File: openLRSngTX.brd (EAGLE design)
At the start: 50 x 40 mm, 29 parts, among them IC1 RFM23BPSMD, J1 AVR_SPI_PRG_6PTH, Q1 MMBT2222, U1 ATMEGA328P, X1 BU-SMA-V, Y1 16MHz

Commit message: Add Open Hardware logo
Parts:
- added U$1: (no value), SparkFun-Aesthetics:OSHW-LOGO-L
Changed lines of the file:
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@@
 </element>
 <element name="R7" library="SparkFun-Resistors" package="0402-RES" value="1k" x="2.794" y="30.48" rot="R270"/>
+<element name="U$1" library="SparkFun-Aesthetics" package="OSHW-LOGO-L" value="" x="43.942" y="18.288" rot="MR0"/>
 </elements>
 <signals>

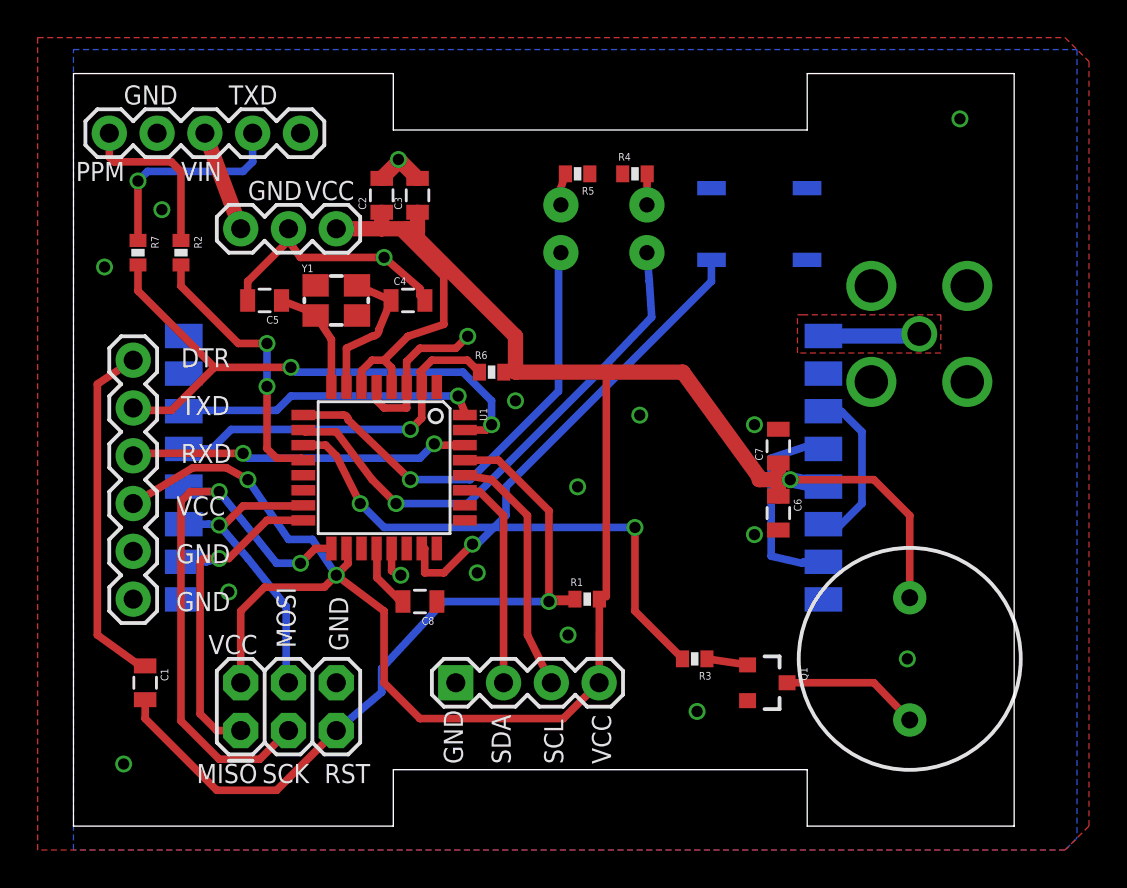
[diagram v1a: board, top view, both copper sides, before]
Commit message: Add mode switch header and room for the actual switch.
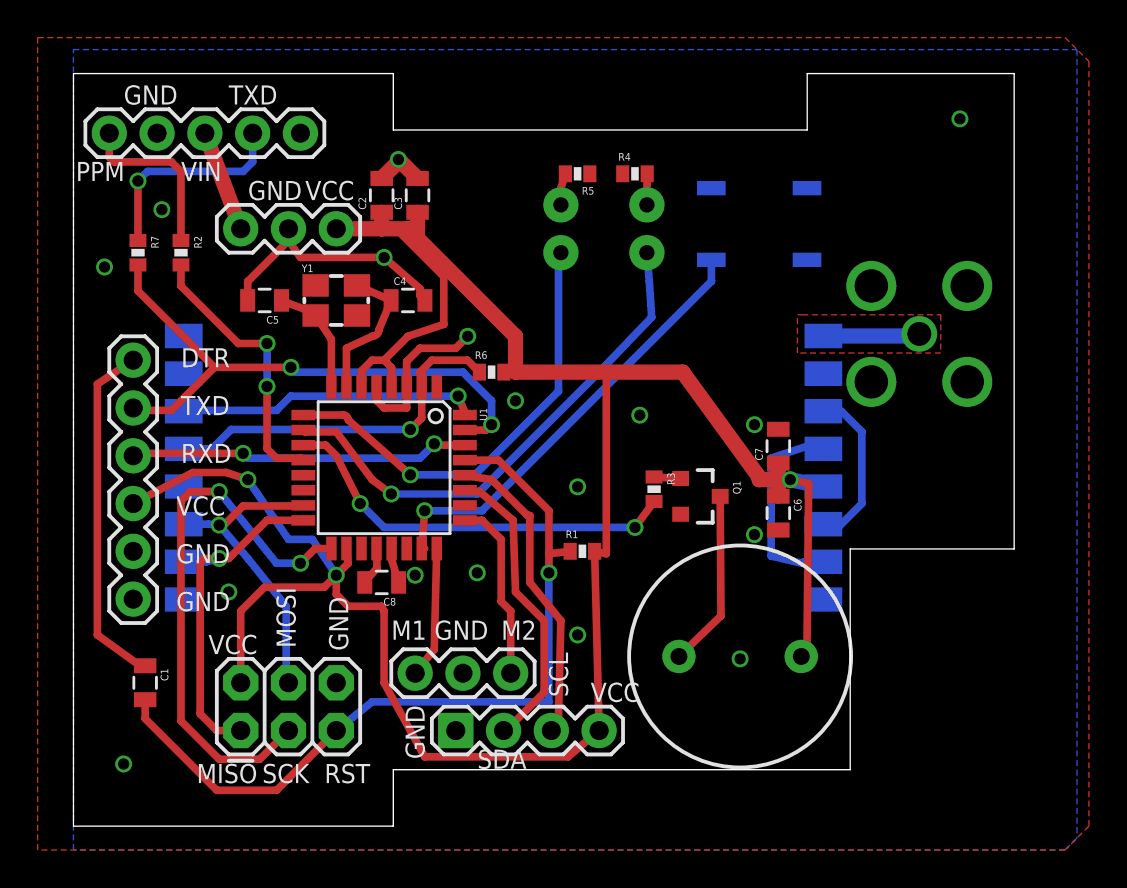
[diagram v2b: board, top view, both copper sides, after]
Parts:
- added JP5: mode, SparkFun-Connectors:1X03
- moved Q1 10.5 mm to (32.6, 17.5)
- moved R3 9.27 mm to (30.2, 17.9), turned to 270 degrees
- moved SG1 9.02 mm to (34.8, 9.02), turned to 0 degrees
- moved R1 2.55 mm to (26.4, 14.6)
- moved JP3 2.54 mm to (19.7, 5.08)
- moved C8 2.27 mm to (15.7, 13.0)
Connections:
- new net N$18: JP5.1, U1.24
- new net N$19: JP5.3, U1.25
- net GND: now also JP5.2
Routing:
- net N$19: track 0.00 -> 9.67 mm
- net N$18: track 0.00 -> 6.99 mm
- net N$4: track 28.0 -> 21.7 mm
- net SDA: track 11.5 -> 15.9 mm
- net VCC: track 126.0 -> 129.7 mm
- net SCL: track 13.3 -> 16.4 mm
- net N$6: track 7.36 -> 9.46 mm
- net N$15: track 25.1 -> 23.6 mm
- net N$14: track 3.45 -> 2.05 mm
- net N$5: track 2.18 -> 1.42 mm
- net /RESET: track 42.2 -> 42.8 mm
- net GND: track 26.8 -> 26.9 mm, vias 18 -> 17
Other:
- outline, holes or cut-outs redrawn
- board text added: "M1"
- board text added: "M2"

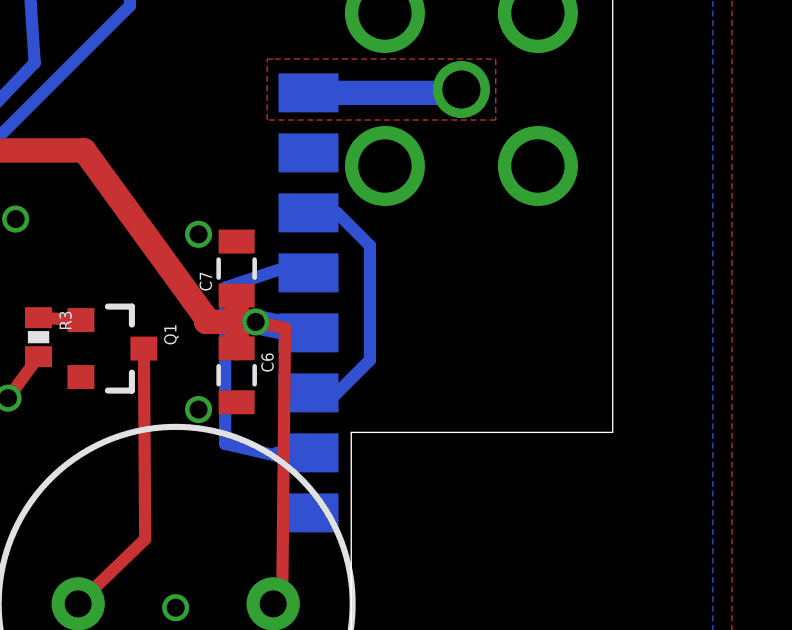
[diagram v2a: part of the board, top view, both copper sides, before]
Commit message: Add logo on other side too.
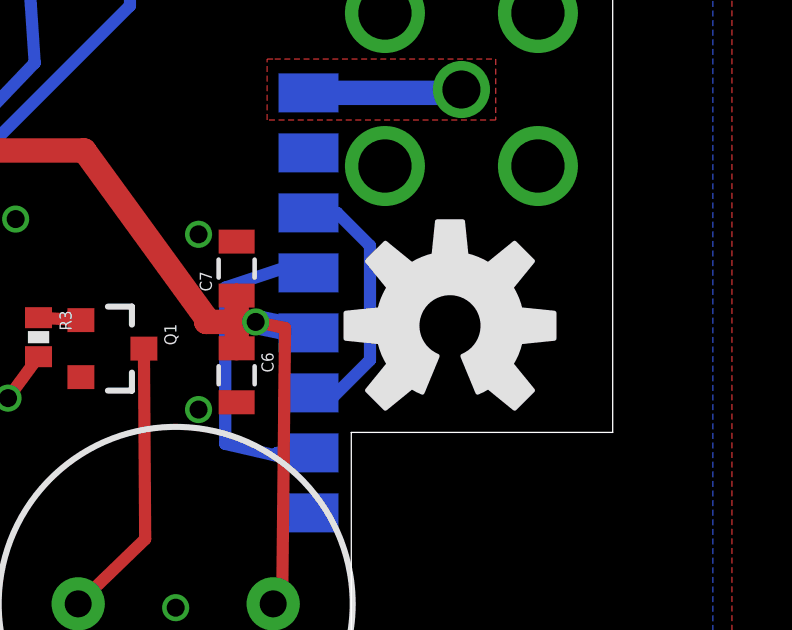
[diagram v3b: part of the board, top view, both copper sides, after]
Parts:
- added U$2: (no value), SparkFun-Aesthetics:OSHW-LOGO-L
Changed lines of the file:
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@@
 <element name="U$1" library="SparkFun-Aesthetics" package="OSHW-LOGO-L" value="" x="43.942" y="18.288" rot="MR0"/>
 <element name="JP5" library="SparkFun-Connectors" package="1X03" value="mode" x="17.526" y="8.128" smashed="yes"/>
+<element name="U$2" library="SparkFun-Aesthetics" package="OSHW-LOGO-L" value="" x="43.942" y="18.288"/>
 </elements>
 <signals>

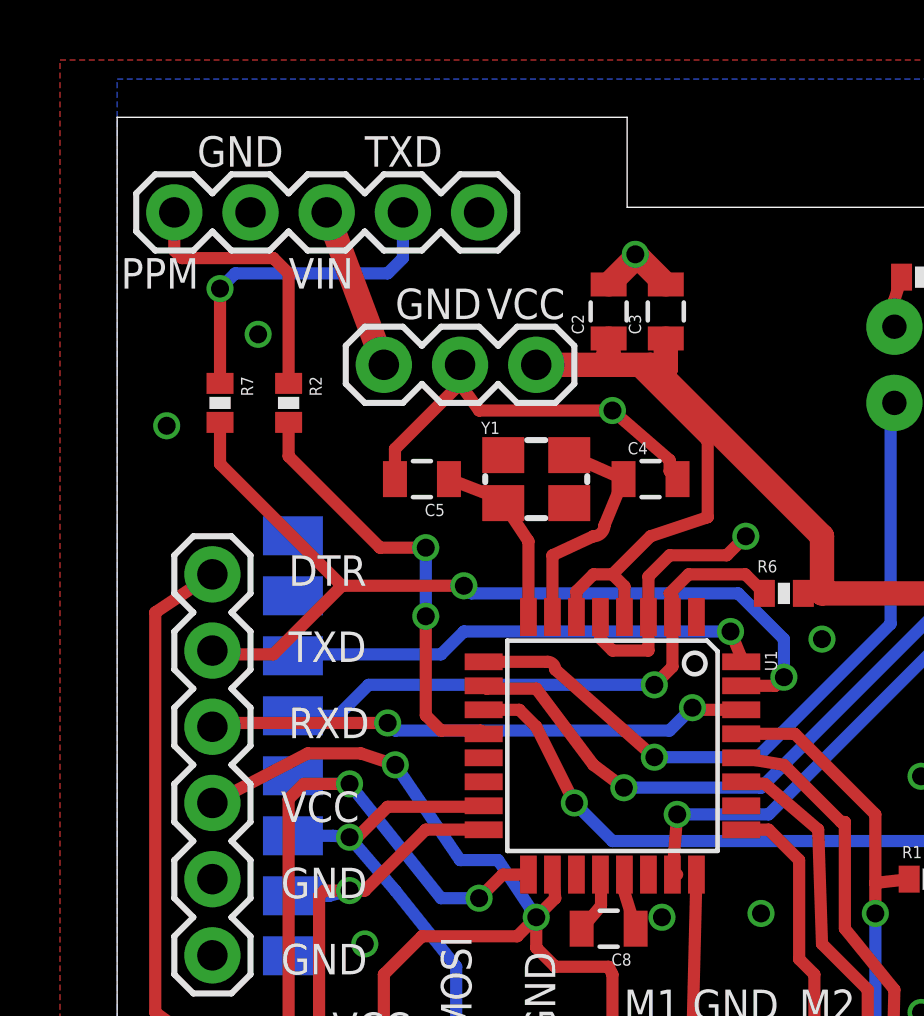
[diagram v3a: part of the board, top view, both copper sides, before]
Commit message: Added connection for RXD towards the radio. Connected xtal case to GND. Performed some routing cleanup.
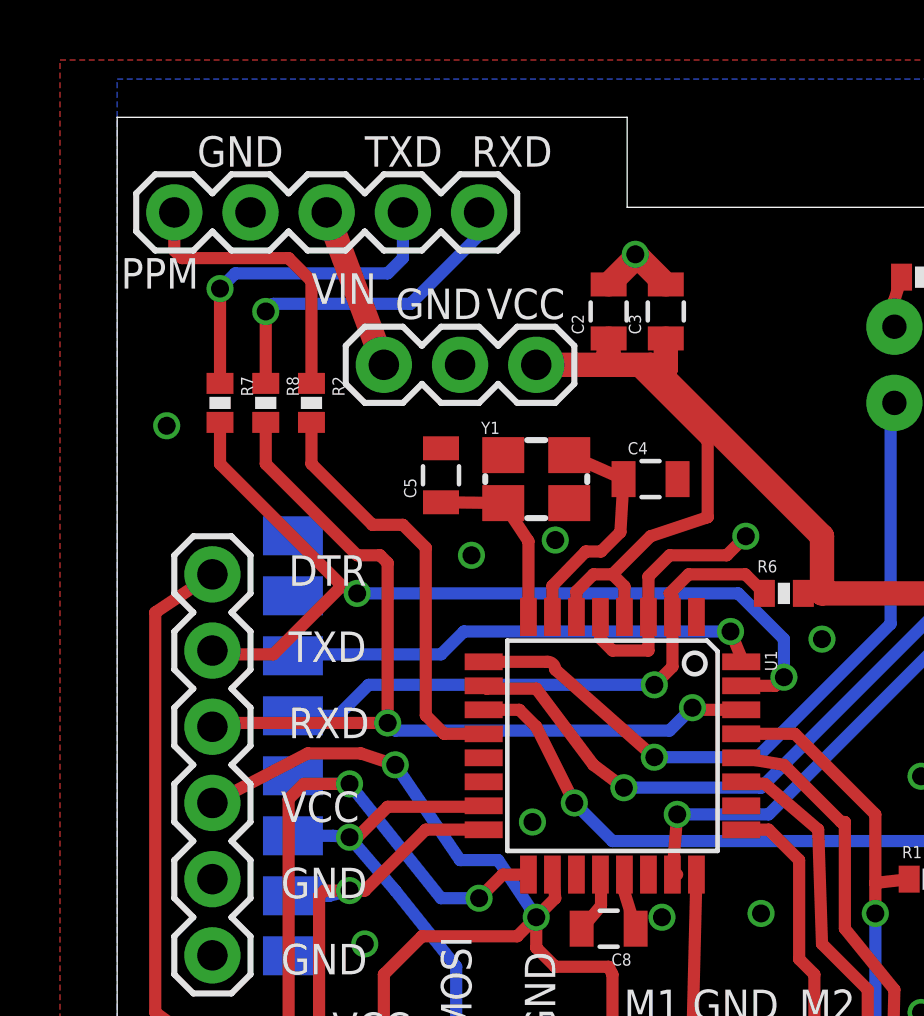
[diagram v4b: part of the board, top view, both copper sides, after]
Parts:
- added R8: 1k, SparkFun-Resistors:0402-RES
- moved R2 0.76 mm to (5.84, 30.5)
- moved C5 0.65 mm to (10.2, 28.1), turned to 90 degrees
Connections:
- new net N$20: JP1.5, R8.1
- net GND: now also Y1.2, Y1.4
- net RXD: now also R8.2
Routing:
- net GND: track 26.9 -> 13.4 mm, vias 17 -> 18
- net RXD: track 18.1 -> 30.3 mm
- net N$20: track 0.00 -> 11.3 mm, vias 0 -> 1
- net N$3: track 9.06 -> 9.68 mm
- net ICP: track 14.7 -> 14.1 mm, vias 2 -> 0
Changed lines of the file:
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@@
 <text x="-0.508" y="34.29" size="1.016" layer="25">PPM</text>
 <text x="2.032" y="38.354" size="1.016" layer="25">GND</text>
-<text x="5.08" y="34.29" size="1.016" layer="25">VIN</text>
+<text x="5.842" y="33.782" size="1.016" layer="25">VIN</text>
 <text x="7.62" y="38.354" size="1.016" layer="25">TXD</text>
 <text x="11.684" y="33.274" size="1.016" layer="25">VCC</text>
@@
 <text x="22.098" y="9.906" size="1.016" layer="25">M2</text>
 <text x="18.542" y="9.906" size="1.016" layer="25">GND</text>
+<text x="11.176" y="38.354" size="1.016" layer="25">RXD</text>
 </plain>
 <attributes>
@@
 <element name="Q1" library="SparkFun-DiscreteSemi" package="SOT23-3" value="MMBT2222" x="32.639" y="17.526" rot="R270"/>
 <element name="R1" library="SparkFun-Resistors" package="0402-RES" value="10k" x="26.416" y="14.605"/>
-<element name="R2" library="SparkFun-Resistors" package="0402-RES" value="1k" x="5.08" y="30.48" rot="R270"/>
+<element name="R2" library="SparkFun-Resistors" package="0402-RES" value="1k" x="5.842" y="30.48" rot="R270"/>
 <element name="R3" library="SparkFun-Resistors" package="0402-RES" value="1k" x="30.226" y="17.907" rot="R270"/>
 <element name="R4" library="SparkFun-Resistors" package="0402-RES" value="220R" x="29.21" y="34.671"/>
@@
 <element name="C3" library="SparkFun-Capacitors" package="0805" value="1uF" x="17.653" y="33.528" rot="R90"/>
 <element name="C4" library="SparkFun-Capacitors" package="0805" value="12pF" x="17.145" y="27.94"/>
-<element name="C5" library="SparkFun-Capacitors" package="0805" value="12pF" x="9.525" y="27.94" rot="R180"/>
+<element name="C5" library="SparkFun-Capacitors" package="0805" value="12pF" x="10.16" y="28.067" rot="R90"/>
 <element name="X1" library="con-coax" package="BU-SMA-V" value="BU-SMA-V" x="44.323" y="26.162" smashed="yes" rot="MR0">
 <attribute name="OC_NEWARK" value="unknown" x="44.323" y="26.162" size="1.778" layer="28" rot="MR0" display="off"/>
@@
 <element name="JP5" library="SparkFun-Connectors" package="1X03" value="mode" x="17.526" y="8.128" smashed="yes"/>
 <element name="U$2" library="SparkFun-Aesthetics" package="OSHW-LOGO-L" value="" x="43.942" y="18.288"/>
+<element name="R8" library="SparkFun-Resistors" package="0402-RES" value="1k" x="4.318" y="30.48" rot="R270"/>
 </elements>
 <signals>
@@
 <vertex x="-0.635" y="-1.27"/>
 </polygon>
-<wire x1="8.625" y1="27.94" x2="8.625" y2="28.945" width="0.4064" layer="1"/>
-<wire x1="8.625" y1="28.945" x2="10.795" y2="31.115" width="0.4064" layer="1"/>
-<wire x1="10.795" y1="31.75" x2="10.795" y2="31.115" width="0.4064" layer="1"/>
-<wire x1="10.795" y1="31.115" x2="11.43" y2="30.226" width="0.4064" layer="1"/>
-<wire x1="11.43" y1="30.226" x2="15.875" y2="30.226" width="0.4064" layer="1"/>
-<wire x1="15.875" y1="30.226" x2="17.78" y2="28.575" width="0.4064" layer="1"/>
-<wire x1="17.78" y1="28.575" x2="17.78" y2="28.205" width="0.4064" layer="1"/>
-<wire x1="17.78" y1="28.205" x2="18.045" y2="27.94" width="0.4064" layer="1"/>
-<via x="15.875" y="30.226" extent="1-16" drill="0.6"/>
 <wire x1="17.075" y1="23.3426" x2="17.075" y2="24.695" width="0.4064" layer="1"/>
 <wire x1="17.075" y1="24.695" x2="17.78" y2="25.4" width="0.4064" layer="1"/>
@@
 <via x="35.56" y="15.494" extent="1-16" drill="0.6"/>
 <via x="7.62" y="12.446" extent="1-16" drill="0.6"/>
-<via x="4.064" y="32.766" extent="1-16" drill="0.6"/>
 <via x="26.162" y="10.16" extent="1-16" drill="0.6"/>
 <via x="26.162" y="18.034" extent="1-16" drill="0.6"/>
@@
 <wire x1="16.275" y1="14.7574" x2="16.256" y2="14.224" width="0.4064" layer="1"/>
 <wire x1="16.256" y1="14.224" x2="16.648" y2="12.954" width="0.4064" layer="1"/>
+<contactref element="Y1" pad="4"/>
+<contactref element="Y1" pad="2"/>
+<contactref element="Y1" pad="4"/>
+<contactref element="Y1" pad="2"/>
+<via x="13.97" y="25.908" extent="1-16" drill="0.6"/>
+<via x="11.176" y="25.4" extent="1-16" drill="0.6"/>
+<via x="13.208" y="16.51" extent="1-16" drill="0.6"/>
 </signal>
 <signal name="VCC">
@@
 <wire x1="18.542" y1="20.32" x2="18.612" y2="20.25" width="0.4064" layer="1"/>
 <wire x1="18.612" y1="20.25" x2="20.1676" y2="20.25" width="0.4064" layer="1"/>
+<contactref element="R8" pad="2"/>
+<wire x1="4.318" y1="29.83" x2="4.318" y2="28.448" width="0.4064" layer="1"/>
+<wire x1="4.318" y1="28.448" x2="7.366" y2="25.4" width="0.4064" layer="1"/>
+<wire x1="7.366" y1="25.4" x2="8.128" y2="25.4" width="0.4064" layer="1"/>
+<wire x1="8.128" y1="25.4" x2="8.382" y2="25.146" width="0.4064" layer="1"/>
+<wire x1="8.382" y1="25.146" x2="8.382" y2="19.812" width="0.4064" layer="1"/>
 </signal>
 <signal name="TXD">
@@
 <wire x1="21.59" y1="21.336" x2="21.59" y2="22.606" width="0.4064" layer="16"/>
 <wire x1="21.59" y1="22.606" x2="20.066" y2="24.13" width="0.4064" layer="16"/>
-<wire x1="20.066" y1="24.13" x2="11.176" y2="24.13" width="0.4064" layer="16"/>
-<wire x1="11.176" y1="24.13" x2="10.922" y2="24.384" width="0.4064" layer="16"/>
-<via x="10.922" y="24.384" extent="1-16" drill="0.6"/>
-<wire x1="10.922" y1="24.384" x2="6.858" y2="24.384" width="0.4064" layer="1"/>
+<wire x1="20.066" y1="24.13" x2="7.366" y2="24.13" width="0.4064" layer="16"/>
+<via x="7.366" y="24.13" extent="1-16" drill="0.6"/>
+<wire x1="7.366" y1="24.13" x2="6.858" y2="24.384" width="0.4064" layer="1"/>
 <wire x1="6.858" y1="24.384" x2="4.572" y2="22.098" width="0.4064" layer="1"/>
 <wire x1="4.572" y1="22.098" x2="2.667" y2="22.098" width="0.4064" layer="1"/>
@@
 <contactref element="U1" pad="12"/>
 <contactref element="R2" pad="2"/>
-<wire x1="11.5824" y1="19.45" x2="11.4744" y2="19.558" width="0.4064" layer="1"/>
-<wire x1="11.4744" y1="19.558" x2="10.16" y2="19.558" width="0.4064" layer="1"/>
-<wire x1="10.16" y1="19.558" x2="9.652" y2="20.066" width="0.4064" layer="1"/>
-<wire x1="9.652" y1="20.066" x2="9.652" y2="23.368" width="0.4064" layer="1"/>
-<via x="9.652" y="23.368" extent="1-16" drill="0.6"/>
-<wire x1="9.652" y1="23.368" x2="9.652" y2="25.654" width="0.4064" layer="16"/>
-<via x="9.652" y="25.654" extent="1-16" drill="0.6"/>
-<wire x1="9.652" y1="25.654" x2="8.128" y2="25.654" width="0.4064" layer="1"/>
-<wire x1="8.128" y1="25.654" x2="5.08" y2="28.702" width="0.4064" layer="1"/>
-<wire x1="5.08" y1="28.702" x2="5.08" y2="29.83" width="0.4064" layer="1"/>
+<wire x1="11.5824" y1="19.45" x2="10.268" y2="19.45" width="0.4064" layer="1"/>
+<wire x1="10.268" y1="19.45" x2="9.652" y2="20.066" width="0.4064" layer="1"/>
+<wire x1="9.652" y1="20.066" x2="9.652" y2="25.654" width="0.4064" layer="1"/>
+<wire x1="9.652" y1="25.654" x2="8.89" y2="26.416" width="0.4064" layer="1"/>
+<wire x1="8.89" y1="26.416" x2="7.874" y2="26.416" width="0.4064" layer="1"/>
+<wire x1="7.874" y1="26.416" x2="5.842" y2="28.448" width="0.4064" layer="1"/>
+<wire x1="5.842" y1="28.448" x2="5.842" y2="29.83" width="0.4064" layer="1"/>
 </signal>
 <signal name="N$3">
 <contactref element="R2" pad="1"/>
 <contactref element="JP1" pad="1"/>
-<wire x1="5.08" y1="31.13" x2="5.08" y2="34.798" width="0.4064" layer="1"/>
-<wire x1="5.08" y1="34.798" x2="4.572" y2="35.306" width="0.4064" layer="1"/>
-<wire x1="4.572" y1="35.306" x2="1.524" y2="35.306" width="0.4064" layer="1"/>
+<wire x1="5.842" y1="31.13" x2="5.842" y2="34.544" width="0.4064" layer="1"/>
+<wire x1="5.842" y1="34.544" x2="5.08" y2="35.306" width="0.4064" layer="1"/>
+<wire x1="5.08" y1="35.306" x2="1.524" y2="35.306" width="0.4064" layer="1"/>
 <wire x1="1.524" y1="35.306" x2="1.27" y2="35.56" width="0.4064" layer="1"/>
 <wire x1="1.27" y1="35.56" x2="1.27" y2="36.83" width="0.4064" layer="1"/>
@@
 <contactref element="U1" pad="7"/>
 <contactref element="Y1" pad="3"/>
-<wire x1="13.875" y1="23.3426" x2="13.875" y2="25.4" width="0.4064" layer="1"/>
-<wire x1="13.875" y1="25.4" x2="15.24" y2="26.035" width="0.4064" layer="1"/>
-<wire x1="15.24" y1="26.035" x2="15.61" y2="26.405" width="0.4064" layer="1" curve="90"/>
-<wire x1="15.61" y1="26.405" x2="16.245" y2="27.94" width="0.4064" layer="1"/>
+<wire x1="13.875" y1="23.3426" x2="13.875" y2="24.384" width="0.4064" layer="1"/>
+<wire x1="13.875" y1="24.384" x2="14.986" y2="25.527" width="0.4064" layer="1"/>
+<wire x1="16.14" y1="26.173" x2="16.245" y2="27.94" width="0.4064" layer="1"/>
 <wire x1="16.245" y1="27.94" x2="14.435" y2="28.74" width="0.4064" layer="1"/>
+<wire x1="14.986" y1="25.527" x2="15.494" y2="25.527" width="0.4064" layer="1"/>
+<wire x1="15.494" y1="25.527" x2="16.14" y2="26.173" width="0.4064" layer="1"/>
 </signal>
 <signal name="N$12">
@@
 <wire x1="13.075" y1="23.3426" x2="13.075" y2="25.87" width="0.4064" layer="1"/>
 <wire x1="13.075" y1="25.87" x2="12.235" y2="27.14" width="0.4064" layer="1"/>
-<wire x1="10.425" y1="27.94" x2="12.495" y2="27.14" width="0.4064" layer="1"/>
+<wire x1="10.16" y1="27.167" x2="12.495" y2="27.14" width="0.4064" layer="1"/>
 <wire x1="12.495" y1="27.14" x2="12.235" y2="27.14" width="0.4064" layer="1"/>
 </signal>
@@
 <wire x1="22.606" y1="11.43" x2="22.606" y2="8.128" width="0.4064" layer="1"/>
 </signal>
+<signal name="N$20">
+<contactref element="R8" pad="1"/>
+<contactref element="JP1" pad="5"/>
+<wire x1="4.318" y1="31.13" x2="4.318" y2="33.528" width="0.4064" layer="1"/>
+<via x="4.318" y="33.528" extent="1-16" drill="0.6"/>
+<wire x1="4.318" y1="33.528" x2="4.572" y2="33.782" width="0.4064" layer="16"/>
+<wire x1="4.572" y1="33.782" x2="9.144" y2="33.782" width="0.4064" layer="16"/>
+<wire x1="9.144" y1="33.782" x2="11.43" y2="36.068" width="0.4064" layer="16"/>
+<wire x1="11.43" y1="36.068" x2="11.43" y2="36.83" width="0.4064" layer="16"/>
+</signal>
 </signals>
